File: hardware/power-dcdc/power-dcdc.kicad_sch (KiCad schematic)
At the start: 65 parts, among them J1 SOLAR_IN, J2 BATT2, J3 BATT1, J4 DCDC-MEASURES, J5 DCDC-PWM, Q1 SIR164ADP, Q2 SIR164ADP, Q3 SI7149ADP, Q4 SI7149ADP, Q5 SI7149ADP, Q6 SI7149ADP, U1 LP4951C, U2 NCP5901B, U3 PAC1953-1, U4 DGD0215, U5 DGD0215

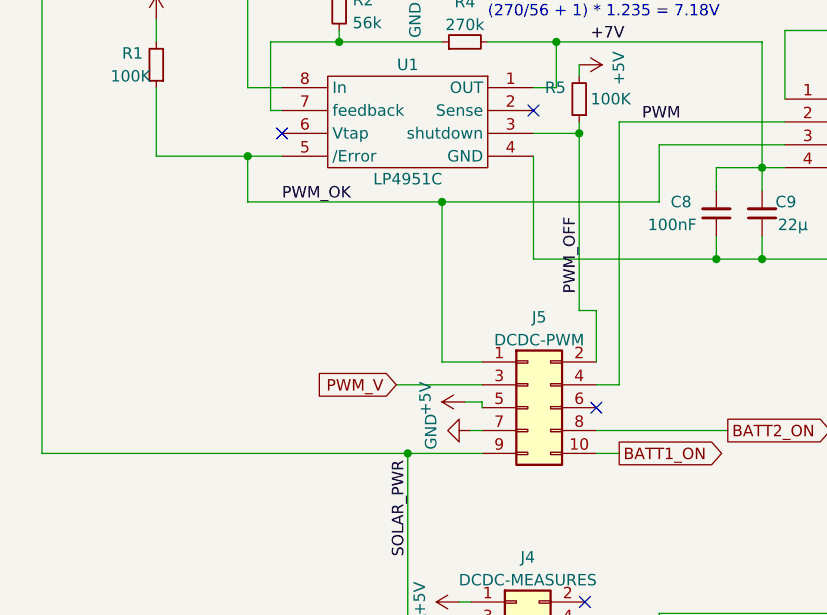
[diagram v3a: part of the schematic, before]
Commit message: Move thermistor to power-dcdc board (measure board temp) Adjust power-dcdc board layout, pass DRC
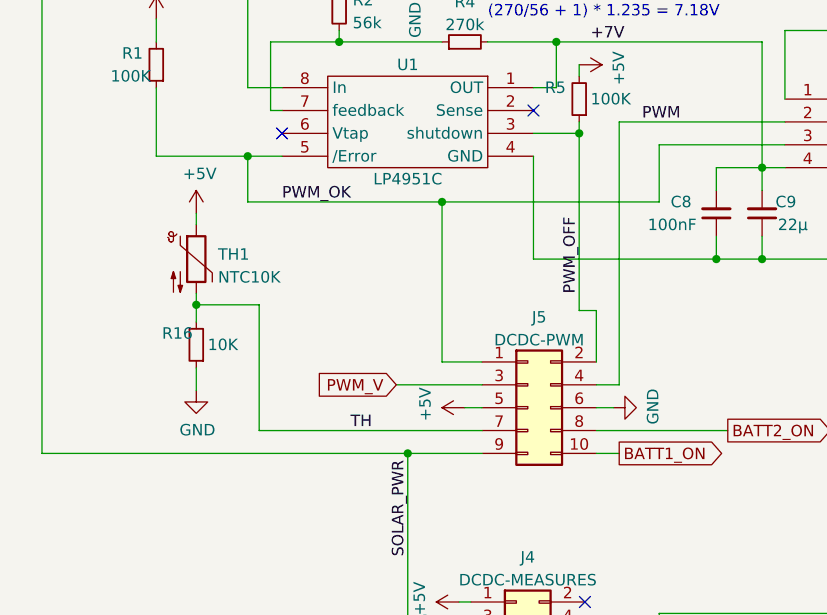
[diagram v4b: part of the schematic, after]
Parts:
- added R16: 10K, Resistor_SMD:R_0805_2012Metric_Pad1.20x1.40mm_HandSolder, symbol Device:R_Small
- added TH1: NTC10K, Resistor_SMD:R_0603_1608Metric_Pad0.98x0.95mm_HandSolder, symbol Device:Thermistor_NTC
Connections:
- net +5V: now also TH1.1
- net GND: now also J5.6 (Pin_6), R16.1; no longer J5.7 (Pin_7)
- new net TH: J5.7 (Pin_7), R16.2, TH1.2
- no-connect marks 6 -> 5
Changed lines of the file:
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@@
   (junction (at 196.85 73.66) (diameter 0) (color 0 0 0 0)
+  )
+  (junction (at 56.515 78.74) (diameter 0) (color 0 0 0 0)
   )
   (junction (at 245.11 83.82) (diameter 0) (color 0 0 0 0)
@@
   (no_connect (at 86.995 116.84))
   (no_connect (at 99.695 114.3))
-  (no_connect (at 100.965 90.17))
   (no_connect (at 99.695 111.76))
   (no_connect (at 66.04 59.69))
   (no_connect (at 93.98 57.15))
+  (wire (pts (xy 56.515 85.725) (xy 56.515 88.265))
+    (stroke (width 0) (type default) (color 0 0 0 0))
+  )
   (wire (pts (xy 269.24 63.5) (xy 269.24 66.04))
     (stroke (width 0) (type default) (color 0 0 0 0))
@@
     (stroke (width 0) (type default) (color 0 0 0 0))
   )
-  (wire (pts (xy 88.265 89.535) (xy 88.265 90.17))
-    (stroke (width 0) (type default) (color 0 0 0 0))
-  )
   (wire (pts (xy 241.3 139.7) (xy 245.11 139.7))
     (stroke (width 0) (type default) (color 0 0 0 0))
@@
     (stroke (width 0) (type default) (color 0 0 0 0))
   )
+  (wire (pts (xy 56.515 77.47) (xy 56.515 78.74))
+    (stroke (width 0) (type default) (color 0 0 0 0))
+  )
   (wire (pts (xy 64.77 49.53) (xy 64.77 57.15))
     (stroke (width 0) (type default) (color 0 0 0 0))
@@
     (stroke (width 0) (type default) (color 0 0 0 0))
   )
-  (wire (pts (xy 86.36 89.535) (xy 88.265 89.535))
+  (wire (pts (xy 86.36 90.17) (xy 88.265 90.17))
     (stroke (width 0) (type default) (color 0 0 0 0))
   )
@@
     (stroke (width 0) (type default) (color 0 0 0 0))
   )
+  (wire (pts (xy 56.515 78.74) (xy 63.5 78.74))
+    (stroke (width 0) (type default) (color 0 0 0 0))
+  )
   (wire (pts (xy 105.41 128.905) (xy 108.585 128.905))
     (stroke (width 0) (type default) (color 0 0 0 0))
@@
     (stroke (width 0) (type default) (color 0 0 0 0))
   )
+  (wire (pts (xy 100.965 90.17) (xy 102.87 90.17))
+    (stroke (width 0) (type default) (color 0 0 0 0))
+  )
   (wire (pts (xy 142.24 120.65) (xy 142.24 121.92))
     (stroke (width 0) (type default) (color 0 0 0 0))
@@
     (stroke (width 0) (type default) (color 0 0 0 0))
   )
+  (wire (pts (xy 56.515 68.58) (xy 56.515 69.85))
+    (stroke (width 0) (type default) (color 0 0 0 0))
+  )
   (wire (pts (xy 62.23 67.31) (xy 83.82 67.31))
     (stroke (width 0) (type default) (color 0 0 0 0))
@@
     (stroke (width 0) (type default) (color 0 0 0 0))
   )
+  (wire (pts (xy 56.515 78.74) (xy 56.515 80.645))
+    (stroke (width 0) (type default) (color 0 0 0 0))
+  )
   (wire (pts (xy 234.95 129.54) (xy 236.22 129.54))
     (stroke (width 0) (type default) (color 0 0 0 0))
@@
     (stroke (width 0) (type default) (color 0 0 0 0))
   )
-  (wire (pts (xy 86.995 92.71) (xy 88.265 92.71))
+  (wire (pts (xy 63.5 92.71) (xy 88.265 92.71))
     (stroke (width 0) (type default) (color 0 0 0 0))
   )
   (wire (pts (xy 250.19 142.24) (xy 250.19 146.05))
+    (stroke (width 0) (type default) (color 0 0 0 0))
+  )
+  (wire (pts (xy 63.5 78.74) (xy 63.5 92.71))
     (stroke (width 0) (type default) (color 0 0 0 0))
   )
@@
   )
   (label "~{PAC_DOWN}" (at 163.83 129.54 90)
+    (effects (font (size 1.27 1.27)) (justify left bottom))
+  )
+  (label "TH" (at 73.66 92.71 0)
     (effects (font (size 1.27 1.27)) (justify left bottom))
   )
@@
     )
   )
-  (symbol (lib_id "power:GND") (at 86.995 92.71 270) (unit 1)
-    (in_bom yes) (on_board yes)
-    (property "Reference" "#PWR020" (id 0) (at 80.645 92.71 0)
-      (effects (font (size 1.27 1.27)) hide)
-    )
-    (property "Value" "GND" (id 1) (at 82.6008 92.837 0))
-    (property "Footprint" "" (id 2) (at 86.995 92.71 0)
-      (effects (font (size 1.27 1.27)) hide)
-    )
-    (property "Datasheet" "" (id 3) (at 86.995 92.71 0)
+  (symbol (lib_id "power:GND") (at 102.87 90.17 90) (unit 1)
+    (in_bom yes) (on_board yes)
+    (property "Reference" "#PWR020" (id 0) (at 109.22 90.17 0)
+      (effects (font (size 1.27 1.27)) hide)
+    )
+    (property "Value" "GND" (id 1) (at 107.2642 90.043 0))
+    (property "Footprint" "" (id 2) (at 102.87 90.17 0)
+      (effects (font (size 1.27 1.27)) hide)
+    )
+    (property "Datasheet" "" (id 3) (at 102.87 90.17 0)
       (effects (font (size 1.27 1.27)) hide)
     )
@@
     (pin "1")
   )
+  (symbol (lib_id "Device:R_Small") (at 56.515 83.185 180) (unit 1)
+    (in_bom yes) (on_board yes)
+    (property "Reference" "R16" (id 0) (at 52.705 81.915 0)
+      (effects (font (size 1.27 1.27)) (justify right))
+    )
+    (property "Value" "10K" (id 1) (at 57.785 83.185 0)
+      (effects (font (size 1.27 1.27)) (justify right))
+    )
+    (property "Footprint" "Resistor_SMD:R_0805_2012Metric_Pad1.20x1.40mm_HandSolder" (id 2) (at 56.515 83.185 0)
+      (effects (font (size 1.27 1.27)) hide)
+    )
+    (property "Datasheet" "~" (id 3) (at 56.515 83.185 0)
+      (effects (font (size 1.27 1.27)) hide)
+    )
+    (pin "1")
+    (pin "2")
+  )
   (symbol (lib_id "Device:R_Shunt") (at 80.01 144.78 0) (unit 1)
     (in_bom yes) (on_board yes)
@@
     (pin "2")
   )
+  (symbol (lib_id "Device:Thermistor_NTC") (at 56.515 73.66 0) (unit 1)
+    (in_bom yes) (on_board yes) (fields_autoplaced)
+    (property "Reference" "TH1" (id 0) (at 58.928 73.1428 0)
+      (effects (font (size 1.27 1.27)) (justify left))
+    )
+    (property "Value" "NTC10K" (id 1) (at 58.928 75.6797 0)
+      (effects (font (size 1.27 1.27)) (justify left))
+    )
+    (property "Footprint" "Resistor_SMD:R_0603_1608Metric_Pad0.98x0.95mm_HandSolder" (id 2) (at 56.515 72.39 0)
+      (effects (font (size 1.27 1.27)) hide)
+    )
+    (property "Datasheet" "~" (id 3) (at 56.515 72.39 0)
+      (effects (font (size 1.27 1.27)) hide)
+    )
+    (property "P/N" " NT06104F3950B1H " (id 4) (at 56.515 73.66 0)
+      (effects (font (size 1.27 1.27)) hide)
+    )
+    (pin "1")
+    (pin "2")
+  )
+  (symbol (lib_id "power:+5V") (at 56.515 68.58 0) (unit 1)
+    (in_bom yes) (on_board yes)
+    (property "Reference" "#PWR0102" (id 0) (at 56.515 72.39 0)
+      (effects (font (size 1.27 1.27)) hide)
+    )
+    (property "Value" "+5V" (id 1) (at 56.896 64.1858 0))
+    (property "Footprint" "" (id 2) (at 56.515 68.58 0)
+      (effects (font (size 1.27 1.27)) hide)
+    )
+    (property "Datasheet" "" (id 3) (at 56.515 68.58 0)
+      (effects (font (size 1.27 1.27)) hide)
+    )
+    (pin "1")
+  )
   (symbol (lib_id "Connector:Screw_Terminal_01x02") (at 43.18 143.51 0) (mirror y) (unit 1)
     (in_bom yes) (on_board yes)
@@
     (pin "2")
   )
-  (symbol (lib_id "power:+5V") (at 86.36 89.535 90) (unit 1)
-    (in_bom yes) (on_board yes)
-    (property "Reference" "#PWR018" (id 0) (at 90.17 89.535 0)
-      (effects (font (size 1.27 1.27)) hide)
-    )
-    (property "Value" "+5V" (id 1) (at 81.9658 89.154 0))
-    (property "Footprint" "" (id 2) (at 86.36 89.535 0)
-      (effects (font (size 1.27 1.27)) hide)
-    )
-    (property "Datasheet" "" (id 3) (at 86.36 89.535 0)
+  (symbol (lib_id "power:+5V") (at 86.36 90.17 90) (unit 1)
+    (in_bom yes) (on_board yes)
+    (property "Reference" "#PWR018" (id 0) (at 90.17 90.17 0)
+      (effects (font (size 1.27 1.27)) hide)
+    )
+    (property "Value" "+5V" (id 1) (at 81.9658 89.789 0))
+    (property "Footprint" "" (id 2) (at 86.36 90.17 0)
+      (effects (font (size 1.27 1.27)) hide)
+    )
+    (property "Datasheet" "" (id 3) (at 86.36 90.17 0)
       (effects (font (size 1.27 1.27)) hide)
     )
@@
     (pin "2")
   )
+  (symbol (lib_id "power:GND") (at 56.515 88.265 0) (unit 1)
+    (in_bom yes) (on_board yes)
+    (property "Reference" "#PWR0101" (id 0) (at 56.515 94.615 0)
+      (effects (font (size 1.27 1.27)) hide)
+    )
+    (property "Value" "GND" (id 1) (at 56.642 92.6592 0))
+    (property "Footprint" "" (id 2) (at 56.515 88.265 0)
+      (effects (font (size 1.27 1.27)) hide)
+    )
+    (property "Datasheet" "" (id 3) (at 56.515 88.265 0)
+      (effects (font (size 1.27 1.27)) hide)
+    )
+    (pin "1")
+  )
   (symbol (lib_id "power:PWR_FLAG") (at 53.34 138.43 0) (unit 1)
     (in_bom yes) (on_board yes) (fields_autoplaced)
@@
       (reference "#PWR020") (unit 1) (value "GND") (footprint "")
     )
+    (path "/eee04e32-29c4-40c0-b299-9b97e6015a6c"
+      (reference "#PWR0101") (unit 1) (value "GND") (footprint "")
+    )
+    (path "/a989f644-a2a4-454f-9c93-5720df6596b6"
+      (reference "#PWR0102") (unit 1) (value "+5V") (footprint "")
+    )
     (path "/e2f6369a-02b5-4d5b-ba47-235a0926e866"
       (reference "C1") (unit 1) (value "YFF31HC") (footprint "local:C_filter_1206")
@@
       (reference "R15") (unit 1) (value "22k") (footprint "Resistor_SMD:R_0805_2012Metric_Pad1.20x1.40mm_HandSolder")
     )
+    (path "/6aa5a5f9-e7a2-40cb-ba4c-8c4c4d11b756"
+      (reference "R16") (unit 1) (value "10K") (footprint "Resistor_SMD:R_0805_2012Metric_Pad1.20x1.40mm_HandSolder")
+    )
+    (path "/a344c995-e9f0-4656-a268-9dcc3bd6cffb"
+      (reference "TH1") (unit 1) (value "NTC10K") (footprint "Resistor_SMD:R_0603_1608Metric_Pad0.98x0.95mm_HandSolder")
+    )
     (path "/e5258ab1-e198-4398-92f3-039abec59fd7"

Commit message: Re-route PCBs to move RJ45 connectors on bottom, saving a bit of stack size.
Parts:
- J4, J5: P/N (none) -> SSW-105-01-T-D
- R7: footprint Resistor_THT:R_Axial_DIN0309_L9.0mm_D3.2mm_P12.70mm_Horizontal -> Resistor_SMD:R_0805_2012Metric_Pad1.20x1.40mm_HandSolder
- R8: footprint Resistor_SMD:R_0805_2012Metric_Pad1.20x1.40mm_HandSolder -> Resistor_THT:R_Axial_DIN0309_L9.0mm_D3.2mm_P12.70mm_Horizontal
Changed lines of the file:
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@@
       (effects (font (size 1.27 1.27)) (justify right))
     )
-    (property "Footprint" "Resistor_THT:R_Axial_DIN0309_L9.0mm_D3.2mm_P12.70mm_Horizontal" (id 2) (at 118.11 124.46 0)
+    (property "Footprint" "Resistor_SMD:R_0805_2012Metric_Pad1.20x1.40mm_HandSolder" (id 2) (at 118.11 124.46 0)
       (effects (font (size 1.27 1.27)) hide)
     )
@@
       (effects (font (size 1.27 1.27)) (justify right))
     )
-    (property "Footprint" "Resistor_SMD:R_0805_2012Metric_Pad1.20x1.40mm_HandSolder" (id 2) (at 158.75 124.46 0)
+    (property "Footprint" "Resistor_THT:R_Axial_DIN0309_L9.0mm_D3.2mm_P12.70mm_Horizontal" (id 2) (at 158.75 124.46 0)
       (effects (font (size 1.27 1.27)) hide)
     )
@@
     )
     (property "Datasheet" "~" (id 3) (at 93.345 90.17 0)
+      (effects (font (size 1.27 1.27)) hide)
+    )
+    (property "P/N" " SSW-105-01-T-D " (id 4) (at 93.345 90.17 0)
       (effects (font (size 1.27 1.27)) hide)
     )
@@
       (effects (font (size 1.27 1.27)) hide)
     )
+    (property "P/N" " SSW-105-01-T-D" (id 4) (at 92.075 116.84 0)
+      (effects (font (size 1.27 1.27)) hide)
+    )
     (pin "1")
     (pin "10")
@@
     )
     (path "/1e11e7ee-1d09-4317-81f3-9082abf4db7f"
-      (reference "R7") (unit 1) (value "10K") (footprint "Resistor_THT:R_Axial_DIN0309_L9.0mm_D3.2mm_P12.70mm_Horizontal")
+      (reference "R7") (unit 1) (value "10K") (footprint "Resistor_SMD:R_0805_2012Metric_Pad1.20x1.40mm_HandSolder")
     )
     (path "/47f33c80-6210-49e0-abe8-9697abdd5dd8"
-      (reference "R8") (unit 1) (value "10K") (footprint "Resistor_SMD:R_0805_2012Metric_Pad1.20x1.40mm_HandSolder")
+      (reference "R8") (unit 1) (value "10K") (footprint "Resistor_THT:R_Axial_DIN0309_L9.0mm_D3.2mm_P12.70mm_Horizontal")
     )
     (path "/4f70259a-7e96-41a9-9e7d-3bf8781b99e6"

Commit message: normalise and update P/N, update footprint to match
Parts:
- C10, C19, C7, C8: footprint Capacitor_SMD:C_0805_2012Metric_Pad1.18x1.45mm_HandSolder -> Capacitor_SMD:C_0603_1608Metric_Pad1.08x0.95mm_HandSolder; P/N (none) -> MC0603B104K250CT (stock)
- C11: P/N GRM31CR71H475KA12L -> C1206C104K5RACTU
- C12: footprint Capacitor_SMD:C_1206_3216Metric_Pad1.33x1.80mm_HandSolder -> Capacitor_SMD:C_1210_3225Metric_Pad1.33x2.70mm_HandSolder; P/N GRM31CR71H475KA12L -> GCM32ER71E106KA57L (stock)
- C17, C18: P/N GRM31CR71H475KA12L -> MC0603B104K250CT (stock)
- C2: footprint Capacitor_SMD:C_0805_2012Metric_Pad1.18x1.45mm_HandSolder -> Capacitor_SMD:C_1206_3216Metric_Pad1.33x1.80mm_HandSolder; P/N CL21B104KBCNNWC -> C1206C104K5RACTU
- F1: P/N 0031.8201 -> 0031.8201 (stock)
- F2, F3, F4, F5, F6, F7: P/N MC011422 -> MC011422 (stock)
- J1, J2, J3: P/N MC000054 -> MC000054 (stock)
- Q1, Q2: P/N SIR164ADP-T1-GE3 -> SIR164ADP-T1-GE3
- Q3, Q4, Q5, Q6: value SI7149ADP -> SI7149ADP; P/N SI7149ADP-T1-GE3 -> SIR164ADP-T1-GE3
- R1, R12, R13, R16, R2, R5, R6, R7, R8, R9: P/N (none) -> stock
- R10, R11, R3: P/N WSLF25122L000FEA -> WSLF25122L000FEA (stock)
- U3: P/N (none) -> pac1953 (stock)
- U4, U5: P/N (none) -> DGD0215

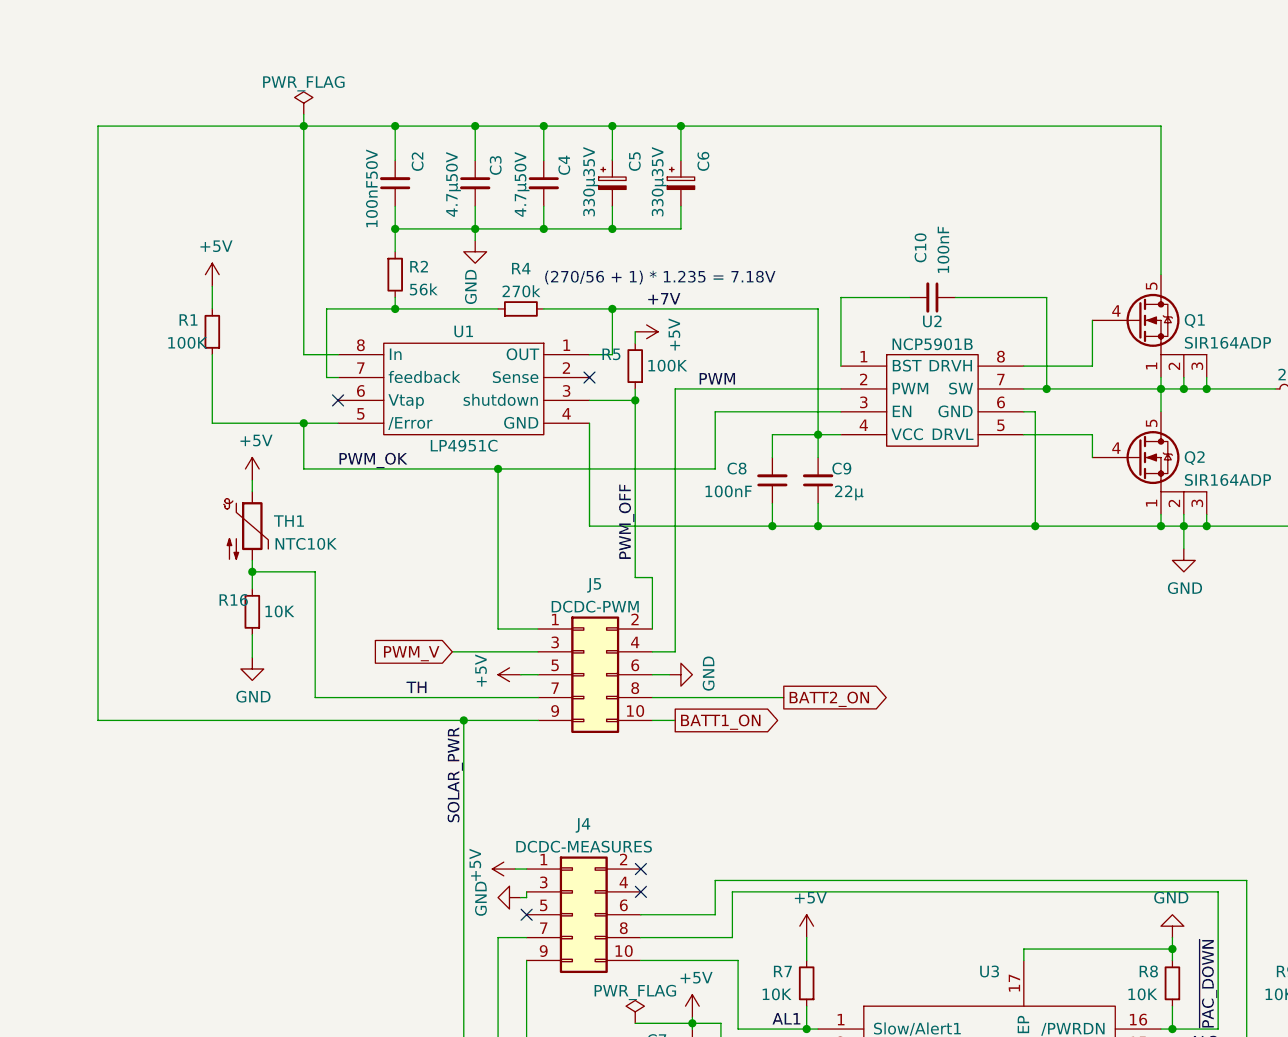
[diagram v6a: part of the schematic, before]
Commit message: On second though, the pac1953  won't be fast enough for the PWM regulation loop. So add a resistor divider routed to RA5 to get the solar voltage from the PIC18's ADC.
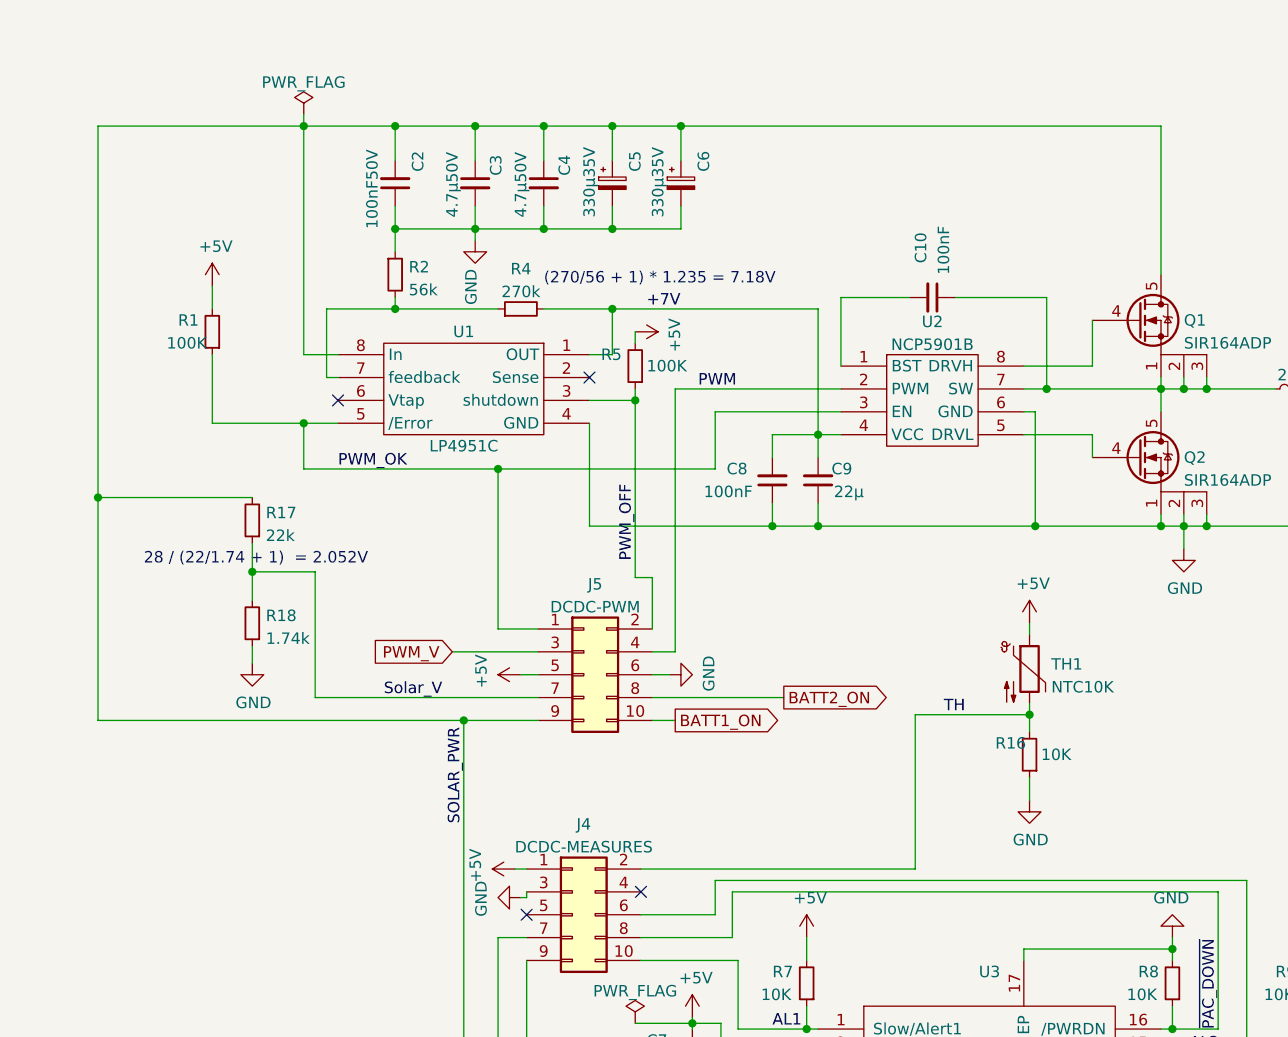
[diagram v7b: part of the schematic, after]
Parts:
- added R17: 22k, Resistor_SMD:R_0805_2012Metric_Pad1.20x1.40mm_HandSolder, symbol Device:R_Small
- added R18: 1.74k, Resistor_SMD:R_0805_2012Metric_Pad1.20x1.40mm_HandSolder, symbol Device:R_Small
- R1, R5: footprint Resistor_THT:R_Axial_DIN0309_L9.0mm_D3.2mm_P12.70mm_Horizontal -> Resistor_THT:R_Axial_DIN0207_L6.3mm_D2.5mm_P10.16mm_Horizontal
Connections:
- net GND: now also R18.1
- net SOLAR_PWR: now also R17.2
- net TH: no longer J5.7 (Pin_7), R16.2, TH1.2
- net at J4.2 (Pin_2): now also R16.2, TH1.2
- new net Solar_V: J5.7 (Pin_7), R17.1, R18.2
- no-connect marks 5 -> 4
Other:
- note added: "28 / (22/1.74 + 1) = 2.052V"
- moved on the sheet: R16, TH1
